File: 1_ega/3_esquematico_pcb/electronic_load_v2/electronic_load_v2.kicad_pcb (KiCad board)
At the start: 2 copper layers, 100 x 50 mm, 68 parts, among them J1 Encoder, J11 LOAD, J12 Memoria SD, J13 LCD, J15 VCC, J16 RTC, J17 EGB, J3 GND, J6 RPico PWR, J7 GND, J8 5V, Q1 IRF540N, Q3 BC327, Q4 BC327, SW1 BTN_MENU, SW2 BTN_STOP, SW3 SW_PWR, U1 LM324, U2 INA219AxD, U3 LM7805_TO220

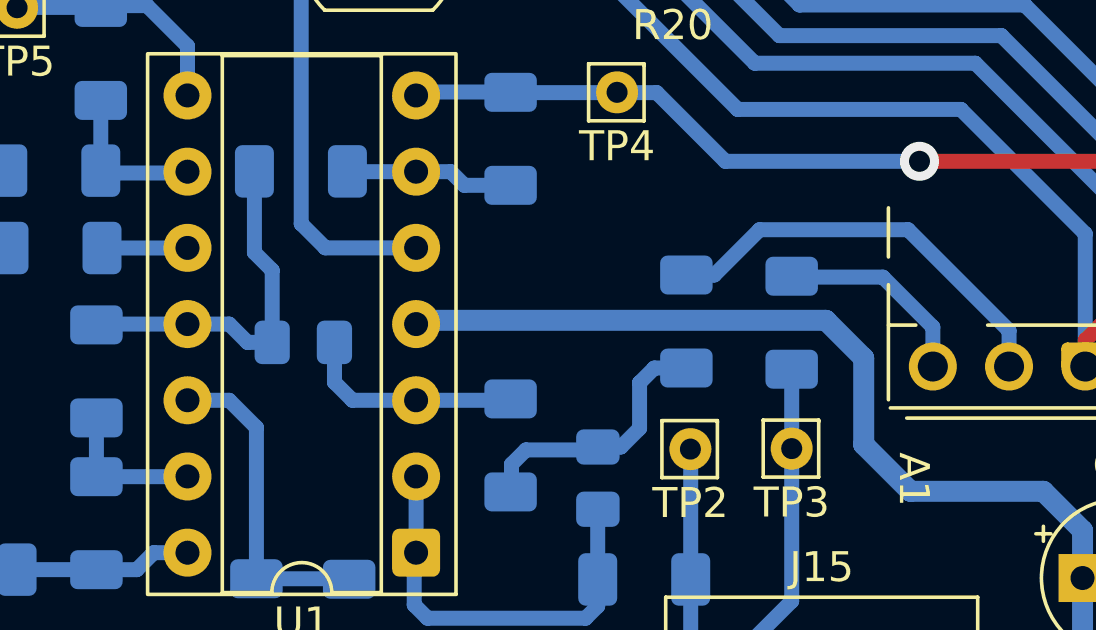
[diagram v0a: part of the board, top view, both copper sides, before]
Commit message: feat: avances ajuste de filtro Sallen Key
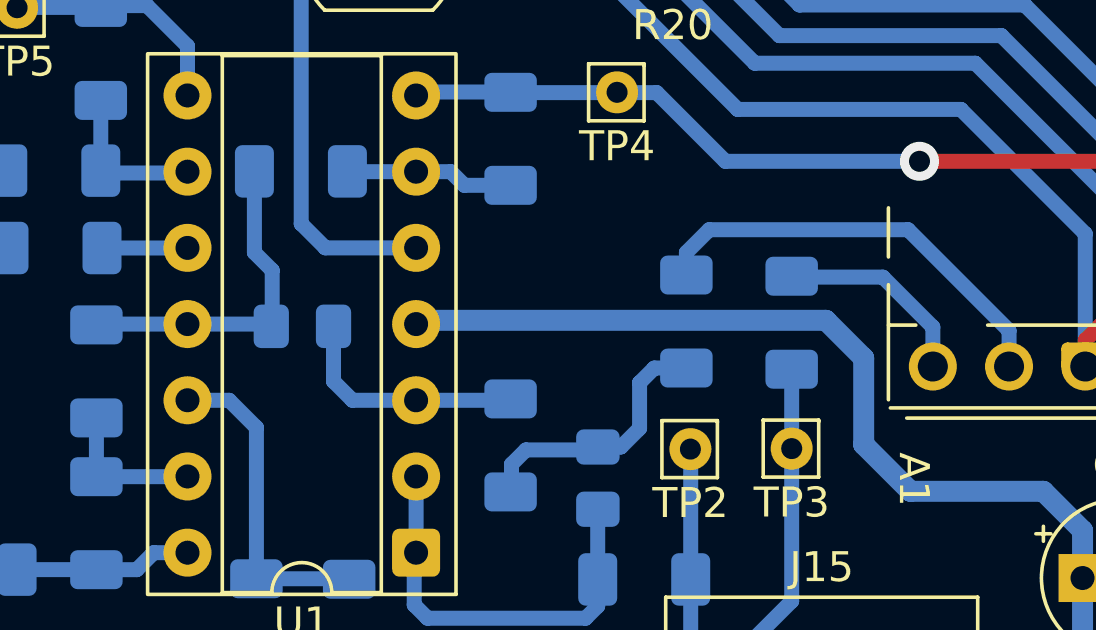
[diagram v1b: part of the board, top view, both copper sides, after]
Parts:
- moved C2 0.54 mm to (47.5, 88.0)
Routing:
- net GND: track 180.4 -> 179.6 mm
- net Net-(U1A-+): track 7.47 -> 8.02 mm
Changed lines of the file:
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@@
 	(footprint "Capacitor_SMD:C_0805_2012Metric_Pad1.18x1.45mm_HandSolder"
 		(layer "B.Cu")
-		(at 47.490165 88.515183 180)
+		(at 47.46 87.98 180)
 		(descr "Capacitor SMD 0805 (2012 Metric), square (rectangular) end terminal, IPC_7351 nominal with elongated pad for handsoldering. (Body size source: IPC-SM-782 page 76, https://www.pcb-3d.com/wordpress/wp-content/uploads/ipc-sm-782a_amendment_1_and_2.pdf, https://docs.google.com/spreadsheets/d/1BsfQQcO9C6DZCsRaXUlFlo91Tg2WpOkGARC1WS5S8t0/edit?usp=sharing), generated with kicad-footprint-generator")
 		(tags "capacitor handsolder")
@@
 	)
 	(segment
-		(start 45.860165 82.815183)
-		(end 45.860165 85.520165)
+		(start 46.452665 86.112665)
+		(end 46.452665 87.949835)
 		(width 0.5)
 		(layer "B.Cu")
@@
 	)
 	(segment
+		(start 45.860165 85.520165)
+		(end 46.452665 86.112665)
+		(width 0.5)
+		(layer "B.Cu")
+		(net 2)
+	)
+	(segment
 		(start 77.55 62.53)
 		(end 79.43 62.53)
@@
 	)
 	(segment
-		(start 46.452665 88.515183)
-		(end 45.630165 88.515183)
+		(start 43.41 69)
+		(end 41.91 67.5)
 		(width 0.5)
 		(layer "B.Cu")
@@
 	)
 	(segment
-		(start 43.41 69)
-		(end 41.91 67.5)
+		(start 46.452665 87.949835)
+		(end 46.4225 87.98)
+		(width 0.5)
+		(layer "B.Cu")
+		(net 2)
+	)
+	(segment
+		(start 46.347683 87.905183)
+		(end 43.630165 87.905183)
 		(width 0.5)
 		(layer "B.Cu")
@@
 	)
 	(segment
-		(start 46.452665 86.112665)
-		(end 46.452665 88.515183)
-		(width 0.5)
-		(layer "B.Cu")
-		(net 2)
-	)
-	(segment
 		(start 42.225 65.425)
 		(end 41.91 65.74)
@@
 	)
 	(segment
+		(start 46.4225 87.98)
+		(end 46.347683 87.905183)
+		(width 0.5)
+		(layer "B.Cu")
+		(net 2)
+	)
+	(segment
 		(start 62.8 69.38)
 		(end 62.8 76.04)
@@
 	)
 	(segment
-		(start 45.860165 85.520165)
-		(end 46.452665 86.112665)
-		(width 0.5)
-		(layer "B.Cu")
-		(net 2)
-	)
-	(segment
 		(start 82.31 100.58)
 		(end 80.4875 98.7575)
@@
 	)
 	(segment
-		(start 45.630165 88.515183)
-		(end 45.020165 87.905183)
-		(width 0.5)
-		(layer "B.Cu")
-		(net 2)
-	)
-	(segment
 		(start 55.26 69)
 		(end 43.41 69)
@@
 	)
 	(segment
+		(start 45.860165 82.815183)
+		(end 45.860165 85.520165)
+		(width 0.5)
+		(layer "B.Cu")
+		(net 2)
+	)
+	(segment
 		(start 41.91 65.74)
 		(end 41.91 70.58)
@@
 	)
 	(segment
-		(start 45.020165 87.905183)
-		(end 43.630165 87.905183)
-		(width 0.5)
-		(layer "B.Cu")
-		(net 2)
-	)
-	(segment
 		(start 86.52 100.55)
 		(end 85.97 100.55)
@@
 	)
 	(segment
-		(start 71.015 88.125)
-		(end 71.015 89.32)
+		(start 67.65 84.76)
+		(end 71.015 88.125)
 		(width 0.5)
 		(layer "B.Cu")
@@
 	)
 	(segment
-		(start 60.26 86.27)
-		(end 61.19 86.27)
+		(start 61.02 84.76)
+		(end 67.65 84.76)
 		(width 0.5)
 		(layer "B.Cu")
@@
 	)
 	(segment
-		(start 67.65 84.76)
-		(end 71.015 88.125)
+		(start 71.015 88.125)
+		(end 71.015 89.32)
 		(width 0.5)
 		(layer "B.Cu")
@@
 	)
 	(segment
-		(start 62.7 84.76)
-		(end 67.65 84.76)
+		(start 60.26 85.52)
+		(end 61.02 84.76)
 		(width 0.5)
 		(layer "B.Cu")
@@
 	)
 	(segment
-		(start 61.19 86.27)
-		(end 62.7 84.76)
+		(start 60.26 86.27)
+		(end 60.26 85.52)
 		(width 0.5)
 		(layer "B.Cu")
@@
 	)
 	(segment
-		(start 49.129096 90.445183)
-		(end 51.250165 90.445183)
+		(start 48.4975 87.98)
+		(end 48.4975 89.813587)
 		(width 0.5)
 		(layer "B.Cu")
@@
 	)
 	(segment
-		(start 48.529096 89.845183)
-		(end 49.129096 90.445183)
+		(start 49.129096 90.445183)
+		(end 51.250165 90.445183)
 		(width 0.5)
 		(layer "B.Cu")
@@
 	)
 	(segment
-		(start 48.529096 88.516614)
-		(end 48.529096 89.845183)
-		(width 0.5)
-		(layer "B.Cu")
-		(net 46)
-	)
-	(segment
-		(start 48.527665 88.515183)
-		(end 48.529096 88.516614)
+		(start 48.4975 89.813587)
+		(end 49.129096 90.445183)
 		(width 0.5)
 		(layer "B.Cu")
